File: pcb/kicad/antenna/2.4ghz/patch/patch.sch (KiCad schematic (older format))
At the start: 1 part, among them P1 CONN_01X02

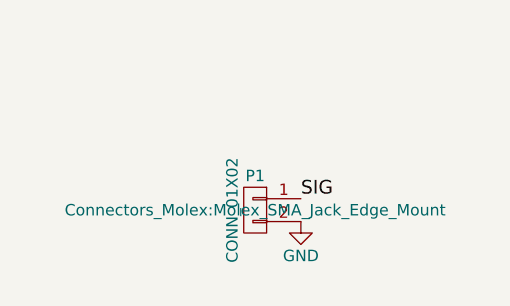
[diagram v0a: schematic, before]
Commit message: Add new revision for patch antenna
New revision shrinks the first revision patch antenna dimensions to
achieve a higher resonance frequency. Feedline was moved closer to the
center to lower the characteristic impedance. The SMA footprint was
edited to remove error with unconnected thermal relief. Layout for the
antenna was simplified with the footprint creator.
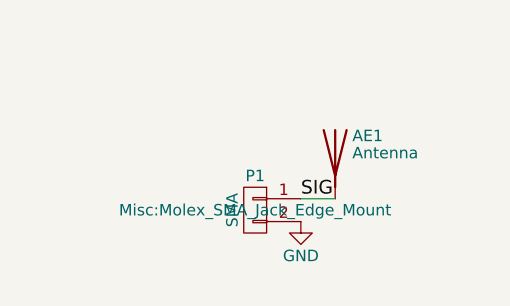
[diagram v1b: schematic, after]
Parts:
- added AE1: Antenna, Antennas:Patch_Antenna_2.4GHz, symbol Antenna
- P1: value CONN_01X02 -> SMA; footprint Connectors_Molex:Molex_SMA_Jack_Edge_Mount -> Misc:Molex_SMA_Jack_Edge_Mount
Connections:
- net SIG: now also AE1.1 (A)
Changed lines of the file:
@@
 P 5500 3600
 F 0 "P1" H 5500 3750 50  0000 C CNN
-F 1 "CONN_01X02" V 5600 3600 50  0000 C CNN
-F 2 "Connectors_Molex:Molex_SMA_Jack_Edge_Mount" H 5500 3600 50  0000 C CNN
+F 1 "SMA" V 5600 3600 50  0000 C CNN
+F 2 "Misc:Molex_SMA_Jack_Edge_Mount" H 5500 3600 50  0000 C CNN
 F 3 "" H 5500 3600 50  0000 C CNN
 	1    5500 3600
@@
 	1    0    0    -1
 $EndComp
+$Comp
+L Antenna AE1
+U 1 1 58C9BCED
+P 5850 3350
+F 0 "AE1" H 5775 3425 50  0000 R CNN
+F 1 "Antenna" H 5775 3350 50  0000 R CNN
+F 2 "Antennas:Patch_Antenna_2.4GHz" H 5850 3350 50  0001 C CNN
+F 3 "" H 5850 3350 50  0001 C CNN
+	1    5850 3350
+	-1   0    0    -1
+$EndComp
+Wire Wire Line
+	5700 3550 5850 3550
 $EndSCHEMATC

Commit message: Add new tests for patch antenna
Two new test boards laid out to test impedance and performance due to
the effect of larger copper void space in the presence of nearby ground
copper, one board with a matching circuit and the other without. Traces
no longer follow the optimal transmission line width for 50ohm
performance due to the use of 0402 SMD technology.
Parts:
- removed AE1: Antenna, Antennas:Patch_Antenna_2.4GHz, symbol Antenna
- added AE1: Antenna_Shield, Antennas:Patch_Antenna_2.4GHz, symbol Antenna_Shield
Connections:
- wire segments 1 -> 3
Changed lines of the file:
@@
 	1    0    0    -1
-$EndComp
-$Comp
-L Antenna AE1
-U 1 1 58C9BCED
-P 5850 3350
-F 0 "AE1" H 5775 3425 50  0000 R CNN
-F 1 "Antenna" H 5775 3350 50  0000 R CNN
-F 2 "Antennas:Patch_Antenna_2.4GHz" H 5850 3350 50  0001 C CNN
-F 3 "" H 5850 3350 50  0001 C CNN
-	1    5850 3350
-	-1   0    0    -1
 $EndComp
 Wire Wire Line
 	5700 3550 5850 3550
+$Comp
+L Antenna_Shield AE1
+U 1 1 58E57C0B
+P 5850 3350
+F 0 "AE1" H 5775 3525 50  0000 R CNN
+F 1 "Antenna_Shield" H 5775 3450 50  0000 R CNN
+F 2 "Antennas:Patch_Antenna_2.4GHz" H 5850 3450 50  0001 C CNN
+F 3 "" H 5850 3450 50  0001 C CNN
+	1    5850 3350
+	1    0    0    -1
+$EndComp
+Wire Wire Line
+	5700 3650 5950 3650
+Wire Wire Line
+	5950 3650 5950 3550
 $EndSCHEMATC
